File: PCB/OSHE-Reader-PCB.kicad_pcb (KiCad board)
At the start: 2 copper layers, 0 parts

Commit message: Actually working now I think
Got new footprints working mainly for the esp
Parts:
- added U1: ESP32-S3-WROOM-1-N8R8, ESP32_S3_WROOM_1_N8R8:XCVR_ESP32S3WROOM1N8R8, F.Cu at (140.9, 83.5)

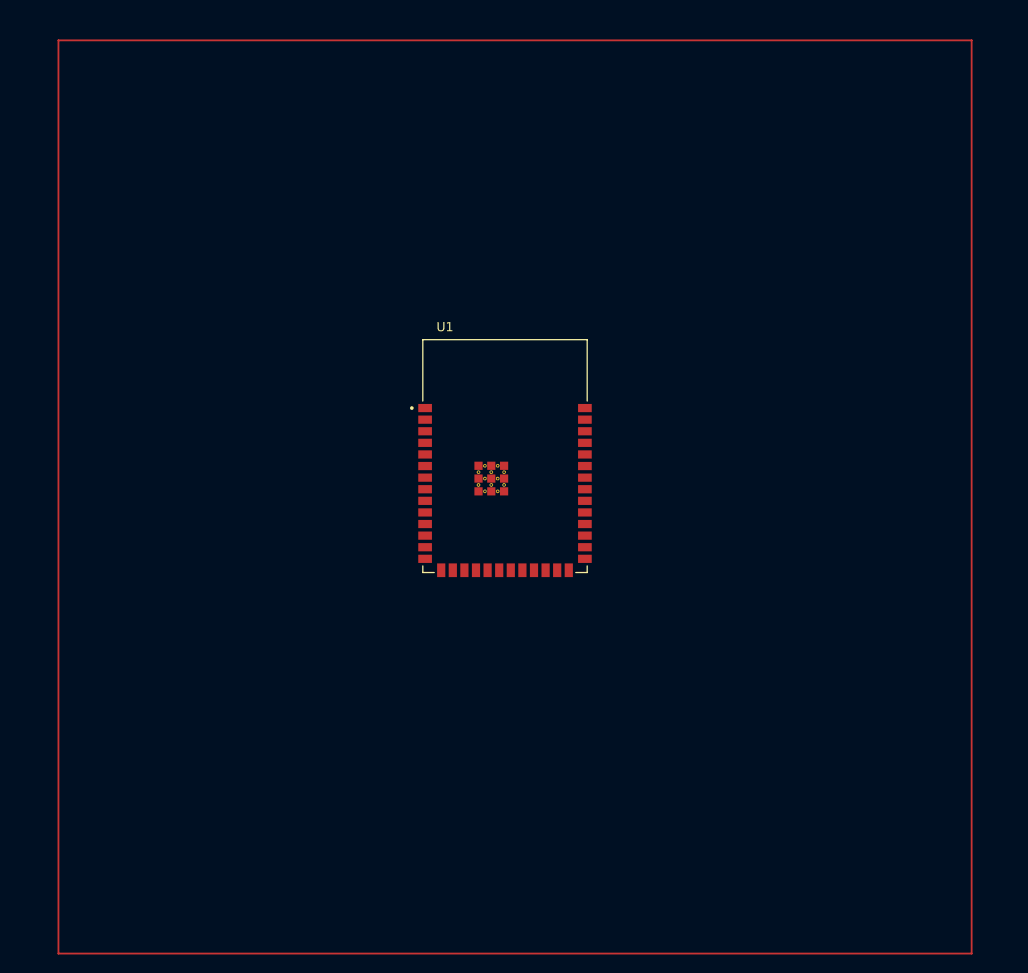
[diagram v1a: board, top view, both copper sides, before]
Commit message: Working on schematic
The display schematic should be done now
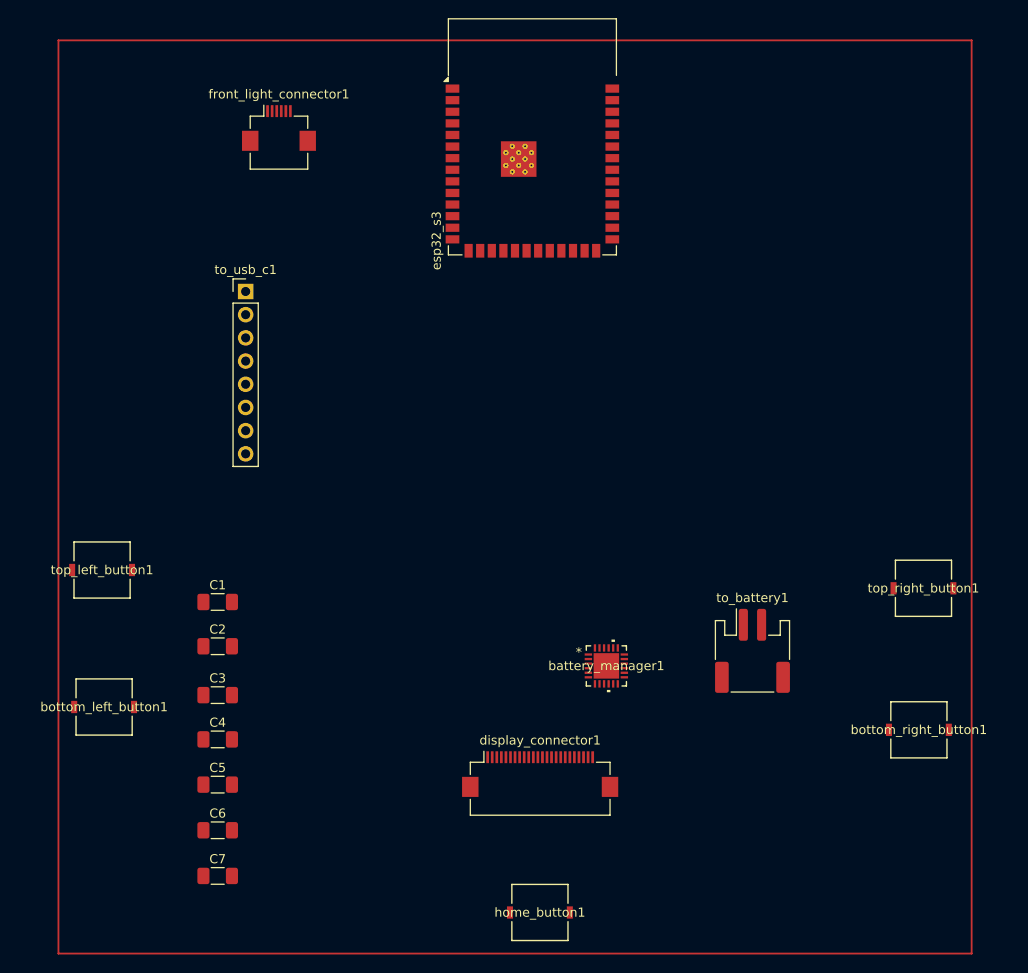
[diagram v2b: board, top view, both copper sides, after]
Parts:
- removed U1: ESP32-S3-WROOM-1-N8R8, ESP32_S3_WROOM_1_N8R8:XCVR_ESP32S3WROOM1N8R8
- added C1: 1uF, Capacitor_SMD:C_1206_3216Metric_Pad1.33x1.80mm_HandSolder, F.Cu at (109.4, 99.5)
- added C2: 1uF, Capacitor_SMD:C_1206_3216Metric_Pad1.33x1.80mm_HandSolder, F.Cu at (109.4, 104.3)
- added C3: 1uF, Capacitor_SMD:C_1206_3216Metric_Pad1.33x1.80mm_HandSolder, F.Cu at (109.4, 109.7)
- added C4: 4.7uF, Capacitor_SMD:C_1206_3216Metric_Pad1.33x1.80mm_HandSolder, F.Cu at (109.4, 114.5)
- added C5: 4.7uF, Capacitor_SMD:C_1206_3216Metric_Pad1.33x1.80mm_HandSolder, F.Cu at (109.4, 119.5)
- added C6: 4.7uF, Capacitor_SMD:C_1206_3216Metric_Pad1.33x1.80mm_HandSolder, F.Cu at (109.4, 124.5)
- added C7: 4.7uF, Capacitor_SMD:C_1206_3216Metric_Pad1.33x1.80mm_HandSolder, F.Cu at (109.4, 129.5)
- added battery_manager1: BQ25616RTWR, BQ25616RTWR:QFN24_RTW_TEX, F.Cu at (152.0, 106.5)
- added bottom_left_button1: 3983, Adafruit 3983:SW_3983_ADA, F.Cu at (97.0, 111.0)
- added bottom_right_button1: 3983, Adafruit 3983:SW_3983_ADA, F.Cu at (186.2, 113.5)
- added display_connector1: Conn_01x24_MountingPin, Connector_FFC-FPC:Hirose_FH12-24S-0.5SH_1x24-1MP_P0.50mm_Horizontal, F.Cu at (144.8, 118.3)
- added esp32_s3: ESP32-S3-WROOM-1-N8R8, RF_Module:ESP32-S3-WROOM-1, F.Cu at (143.9, 48.5)
- added front_light_connector1: Conn_01x06_MountingPin, Connector_FFC-FPC:Hirose_FH12-6S-0.5SH_1x06-1MP_P0.50mm_Horizontal, F.Cu at (116.2, 47.6)
- added home_button1: 3983, Adafruit 3983:SW_3983_ADA, F.Cu at (144.7, 133.5)
- added to_battery1: Conn_01x02_MountingPin, Connector_JST:JST_PH_S2B-PH-SM4-TB_1x02-1MP_P2.00mm_Horizontal, F.Cu at (168.0, 104.8)
- added to_usb_c1: Conn_01x08_Pin, Connector_PinHeader_2.54mm:PinHeader_1x08_P2.54mm_Vertical, F.Cu at (112.5, 65.5)
- added top_left_button1: 3983, Adafruit 3983:SW_3983_ADA, F.Cu at (96.8, 96.0)
- added top_right_button1: 3983, Adafruit 3983:SW_3983_ADA, F.Cu at (186.7, 98.0)

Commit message: Working on PCB
worked on organizing and updating PCB a bit
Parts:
- added C10: 4.7uF, Package_TO_SOT_SMD:SOT-23-6, F.Cu at (146.6, 90.0)
- added C8: 4.7uF, Package_TO_SOT_SMD:SOT-23-6, F.Cu at (123.6, 124.0)
- added C9: 4.7uF, Package_TO_SOT_SMD:SOT-23-6, F.Cu at (164.9, 46.0)
- added D1: MBR0530, Diode_SMD:D_SOD-123, F.Cu at (116.7, 124.0)
- added D2: MBR0530, Diode_SMD:D_SOD-123, F.Cu at (165.0, 53.4)
- added D3: MBR0530, Diode_SMD:D_SOD-123, F.Cu at (123.8, 118.0)
- added L1: 47uH, Package_SO:SOIC-20W_7.5x12.8mm_P1.27mm, F.Cu at (127.8, 76.1)
- added Q1: Si1308EDL, Package_TO_SOT_SMD:SOT-323_SC-70, F.Cu at (123.6, 130.5)
- added R1: 2.2, Package_TO_SOT_SMD:SOT-323_SC-70, F.Cu at (124.4, 112.3)
- moved front_light_connector1 11.3 mm to (104.8, 47.1)
- moved battery_manager1 7.07 mm to (145.0, 105.5)
- moved bottom_right_button1 2.37 mm to (187.5, 111.5)
- moved top_right_button1 2.15 mm to (187.5, 96.0)
- moved bottom_left_button1 0.57 mm to (96.7, 111.5)
- turned C2 to 180 degrees
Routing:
- net GND: track 0.00 -> 30.0 mm

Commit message: Updated PCB a bit
Riley there were 2 C14s very sad
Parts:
- added C13: 10uF, Package_CSP:Xilinx_CSG48_7.0x7.0mm_Layout7x7_P0.8mm, F.Cu at (176.6, 49.1)
- added C14: 4.7uF, Package_CSP:Xilinx_CSG48_7.0x7.0mm_Layout7x7_P0.8mm, F.Cu at (177.1, 60.9)
- added C14*1: 47nF, Package_CSP:Xilinx_CSG48_7.0x7.0mm_Layout7x7_P0.8mm, F.Cu at (177.9, 85.1)
- added C15: 10uF, Package_CSP:Xilinx_CSG48_7.0x7.0mm_Layout7x7_P0.8mm, F.Cu at (177.9, 73.1)
- added D7: LED, LED_SMD:LED_Cree-XHP50_3V_HighDensity, F.Cu at (157.6, 46.2)
- added R3: 10k, Resistor_SMD:R_1206_3216Metric_Pad1.30x1.75mm_HandSolder, F.Cu at (109.5, 92.0)
- added R4: 10k, Resistor_SMD:R_1206_3216Metric_Pad1.30x1.75mm_HandSolder, F.Cu at (110.0, 87.0)
- added R5: 10k, Resistor_SMD:R_1206_3216Metric_Pad1.30x1.75mm_HandSolder, F.Cu at (110.0, 81.5)
- added R6: 10k, Resistor_SMD:R_1206_3216Metric_Pad1.30x1.75mm_HandSolder, F.Cu at (110.5, 75.5)
- added R7: 10k, Resistor_SMD:R_1206_3216Metric_Pad1.30x1.75mm_HandSolder, F.Cu at (111.0, 70.0)
- moved to_usb_c1 15.1 mm to (98.5, 60.0)
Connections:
- net /BUSY renamed /Display + Front Light/BUSY
- net /CS# renamed /Display + Front Light/CS#
- net /D/C# renamed /Display + Front Light/D/C#
- net /GDR renamed /Display + Front Light/GDR
- net /LED_C+ renamed /Display + Front Light/LED_C+
- net /LED_C- renamed /Display + Front Light/LED_C-
- net /LED_W+ renamed /Display + Front Light/LED_W+
- net /LED_W- renamed /Display + Front Light/LED_W-
- net /RES# renamed /Display + Front Light/RES#
- net /RESE renamed /Display + Front Light/RESE
- net /SCL renamed /Display + Front Light/SCL
- net /SDA renamed /Display + Front Light/SDA
- net /VCI renamed /Display + Front Light/VCI
- net /VCOM renamed /Display + Front Light/VCOM
- net /VDD renamed /Display + Front Light/VDD
- net /VGH renamed /Display + Front Light/VGH
- net /VGL renamed /Display + Front Light/VGL
- net /VPP renamed /Display + Front Light/VPP
- net /VSH1 renamed /Display + Front Light/VSH1
- net /VSH2 renamed /Display + Front Light/VSH2
- net /VSL renamed /Display + Front Light/VSL
- battery_manager1 pad 1: /BAT+ -> /VBUS
- battery_manager1 pad 10: unconnected-(battery_manager1-ICHG-Pad10) -> Net-(battery_manager1-ICHG)
- battery_manager1 pad 11: unconnected-(battery_manager1-TS-Pad11) -> /Battery Charger/TS
- battery_manager1 pad 13: unconnected-(battery_manager1-BAT-Pad13) -> /BAT+
- battery_manager1 pad 14: unconnected-(battery_manager1-BAT-Pad14) -> /BAT+
- battery_manager1 pad 15: unconnected-(battery_manager1-SYS-Pad15) -> /Battery Charger/SYS
- battery_manager1 pad 16: unconnected-(battery_manager1-SYS-Pad16) -> /Battery Charger/SYS
- battery_manager1 pad 17: unconnected-(battery_manager1-GND-Pad17) -> GND
- battery_manager1 pad 18: unconnected-(battery_manager1-GND-Pad18) -> GND
- battery_manager1 pad 19: unconnected-(battery_manager1-SW-Pad19) -> /Battery Charger/SW
- battery_manager1 pad 20: unconnected-(battery_manager1-SW-Pad20) -> /Battery Charger/SW
- battery_manager1 pad 21: unconnected-(battery_manager1-BTST-Pad21) -> /Battery Charger/BTST
- battery_manager1 pad 22: unconnected-(battery_manager1-REGN-Pad22) -> /Battery Charger/REGN
- battery_manager1 pad 23: unconnected-(battery_manager1-PMID-Pad23) -> Net-(battery_manager1-PMID)
- battery_manager1 pad 24: unconnected-(battery_manager1-VBUS-Pad24) -> /VBUS
- battery_manager1 pad 5: unconnected-(battery_manager1-STAT-Pad5) -> /Battery Charger/STAT
- battery_manager1 pad 6: unconnected-(battery_manager1-OTG-Pad6) -> /Battery Charger/GPIO_2
- battery_manager1 pad 7: unconnected-(battery_manager1-PG-Pad7) -> /Battery Charger/!PG
- battery_manager1 pad 8: unconnected-(battery_manager1-ILIM-Pad8) -> Net-(battery_manager1-ILIM)
- battery_manager1 pad 9: unconnected-(battery_manager1-CE-Pad9) -> /Battery Charger/GPIO_1
- bottom_left_button1 pad 1: unconnected-(bottom_left_button1-Pad1) -> /BL_button
- bottom_left_button1 pad 2: unconnected-(bottom_left_button1-Pad2) -> GND
- bottom_right_button1 pad 1: unconnected-(bottom_right_button1-Pad1) -> /BR_button
- bottom_right_button1 pad 2: unconnected-(bottom_right_button1-Pad2) -> GND
- esp32_s3 pad 1: unconnected-(esp32_s3-GND-Pad1) -> GND
- esp32_s3 pad 12: unconnected-(esp32_s3-IO8-Pad12) -> /HOME_button
- esp32_s3 pad 2: unconnected-(esp32_s3-3V3-Pad2) -> /3V3
- esp32_s3 pad 4: unconnected-(esp32_s3-IO4-Pad4) -> /BR_button
- esp32_s3 pad 5: unconnected-(esp32_s3-IO5-Pad5) -> /TR_button
- esp32_s3 pad 6: unconnected-(esp32_s3-IO6-Pad6) -> /BL_button
- esp32_s3 pad 7: unconnected-(esp32_s3-IO7-Pad7) -> /TL_button
- home_button1 pad 1: unconnected-(home_button1-Pad1) -> /HOME_button
- home_button1 pad 2: unconnected-(home_button1-Pad2) -> GND
- to_usb_c1 pad 1: /CC2 -> unconnected-(to_usb_c1-Pin_1-Pad1)
- to_usb_c1 pad 2: /SBU1 -> unconnected-(to_usb_c1-Pin_2-Pad2)
- to_usb_c1 pad 5: /CC1 -> unconnected-(to_usb_c1-Pin_5-Pad5)
- to_usb_c1 pad 6: /SBU2 -> unconnected-(to_usb_c1-Pin_6-Pad6)
- to_usb_c1 pad 8: /USB_GND -> GND
- top_left_button1 pad 1: unconnected-(top_left_button1-Pad1) -> /TL_button
- top_left_button1 pad 2: unconnected-(top_left_button1-Pad2) -> GND
- top_right_button1 pad 1: unconnected-(top_right_button1-Pad1) -> /TR_button
- top_right_button1 pad 2: unconnected-(top_right_button1-Pad2) -> GND

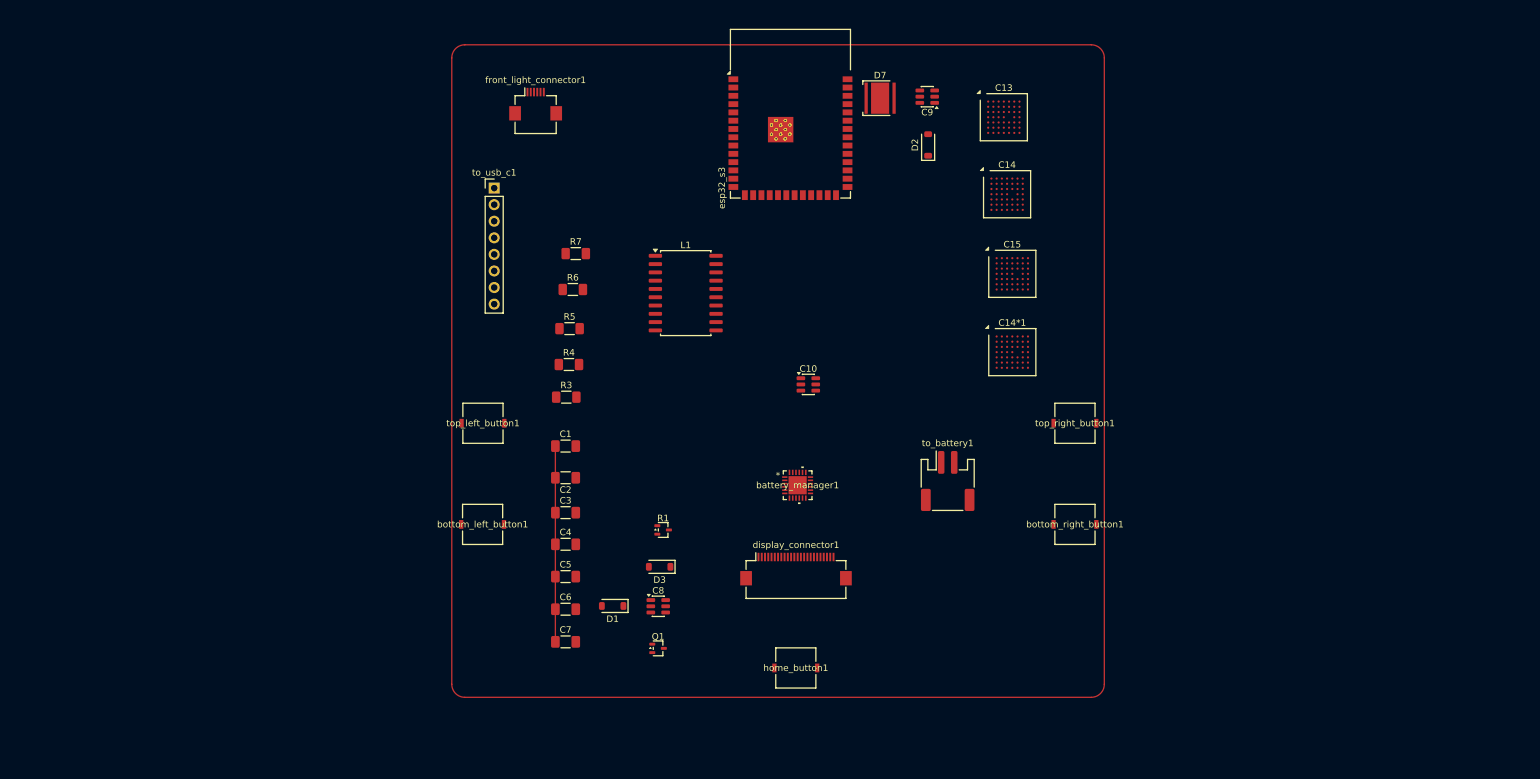
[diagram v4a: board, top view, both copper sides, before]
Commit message: Copied over LED from Silkscreen
LED Power control circuit
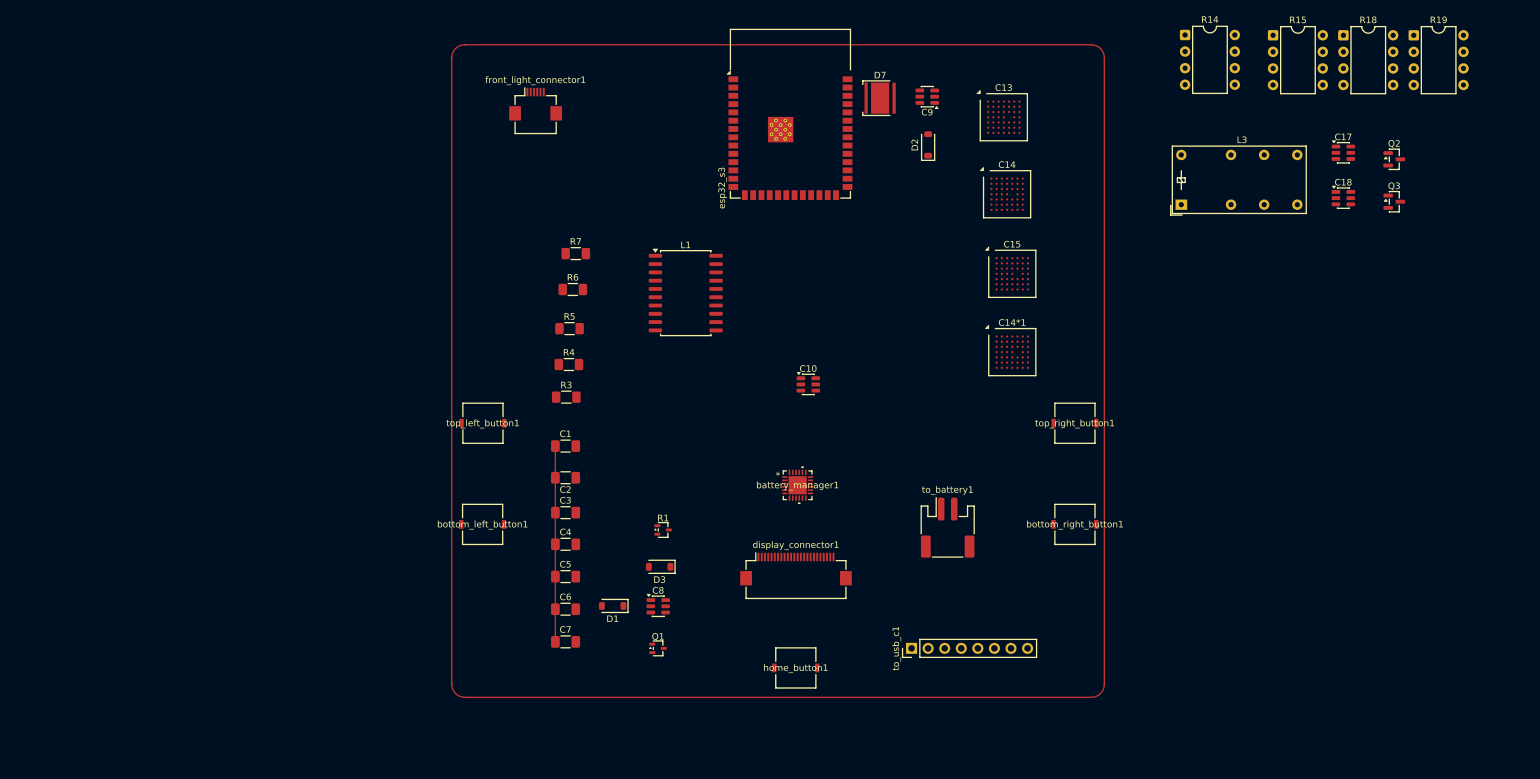
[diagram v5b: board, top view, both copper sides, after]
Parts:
- added C17: 4.7uF, Package_TO_SOT_SMD:SOT-23-6, F.Cu at (228.6, 54.5)
- added C18: 4.7u/50V, Package_TO_SOT_SMD:SOT-23-6, F.Cu at (228.6, 61.5)
- added L3: 10u, Relay_THT:Relay_DPDT_Finder_30.22, F.Cu at (203.8, 62.5)
- added Q2: BSS138, Package_TO_SOT_SMD:SOT-23, F.Cu at (236.4, 55.5)
- added Q3: BSS138, Package_TO_SOT_SMD:SOT-23, F.Cu at (236.4, 62.0)
- added R14: 100k, Package_DIP:DIP-8_W7.62mm, F.Cu at (204.4, 36.5)
- added R15: 1M, Package_DIP:DIP-8_W7.62mm, F.Cu at (217.9, 36.5)
- added R18: 1M, Package_DIP:DIP-8_W7.62mm, F.Cu at (228.6, 36.5)
- added R19: 120k, Package_DIP:DIP-8_W7.62mm, F.Cu at (239.4, 36.5)
- moved to_usb_c1 95.2 mm to (162.5, 130.5), turned to 90 degrees
- moved to_battery1 7.15 mm to (168.0, 112.0)
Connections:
- front_light_connector1 pad 1: /Display + Front Light/LED_W- -> /Display + Front Light/LED_C+
